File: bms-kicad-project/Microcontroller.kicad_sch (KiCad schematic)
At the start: 41 parts, among them J2 Conn_01x02, J3 USB_B_Micro, J4 Conn_02x18_Odd_Even, J5 Conn_02x18_Odd_Even, J6 12402012E212A, U2 NCP1117-3.3_SOT223, U3 W25Q128JVS, U4 RP2040, U5 NCP1117ST33T3G, U6 W25Q128JVSIQ TR, Y1 ABM8-272-T3

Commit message: feat: continuing work on MCU circuit
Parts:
- removed C10, C11: 10u, Capacitor_SMD:C_0805_2012Metric, symbol Device:C
- removed C27, C28: 1µ, FixedWing:CAPC2012X140N, symbol FixedWing:GCM21BR71C105KA58L
- removed J3: USB_B_Micro, RP2040_minimal:USB_Micro-B_Amphenol_10103594-0001LF_Horizontal_modified, symbol Connector:USB_B_Micro
- removed R30: DNF, Resistor_SMD:R_0402_1005Metric, symbol Device:R
- removed U2: NCP1117-3.3_SOT223, Package_TO_SOT_SMD:SOT-223-3_TabPin2, symbol Regulator_Linear:NCP1117-3.3_SOT223
- removed U6: W25Q128JVSIQ TR, FixedWing:SOIC_208MIL_WIN, symbol FixedWing:W25Q128JVSIQ_TR
- added CR1: MBR120VLSFT1G, FixedWing:DIOM3616X98N, symbol FixedWing:MBR120VLSFT1G
- added Q7: BSS308PE_H6327, SOT95P260X110-3N, symbol FixedWing:BSS308PE_H6327
- added R32, R33: 3k3, RESC2012X50N, symbol FixedWing:CRCW08053K30JNEA
- added R? (x4): 1k, FixedWing:RC0805N_YAG, symbol FixedWing:RC0805FR-071KL
- C?: renamed from C12; value 100n -> 0.1µ; footprint Capacitor_SMD:C_0402_1005Metric -> FixedWing:CAP_GCJ-18_MUR; symbol Device:C -> FixedWing:GCJ188R72A104KA01D; Manufacturer (none) -> Murata Electronics; Manufacturer_Part_Number (none) -> GCJ188R72A104KA01D
- C?: renamed from C16; value 100n -> 0.1µ; footprint Capacitor_SMD:C_0402_1005Metric -> FixedWing:CAP_GCJ-18_MUR; symbol Device:C -> FixedWing:GCJ188R72A104KA01D; Manufacturer (none) -> Murata Electronics; Manufacturer_Part_Number (none) -> GCJ188R72A104KA01D
- C?: renamed from C18; value 100n -> 0.1µ; footprint Capacitor_SMD:C_0402_1005Metric -> FixedWing:CAP_GCJ-18_MUR; symbol Device:C -> FixedWing:GCJ188R72A104KA01D; Manufacturer (none) -> Murata Electronics; Manufacturer_Part_Number (none) -> GCJ188R72A104KA01D
- C?: renamed from C19; value 100n -> 0.1µ; footprint Capacitor_SMD:C_0402_1005Metric -> FixedWing:CAP_GCJ-18_MUR; symbol Device:C -> FixedWing:GCJ188R72A104KA01D; Manufacturer (none) -> Murata Electronics; Manufacturer_Part_Number (none) -> GCJ188R72A104KA01D
- C?: renamed from C20; value 100n -> 0.1µ; footprint Capacitor_SMD:C_0402_1005Metric -> FixedWing:CAP_GCJ-18_MUR; symbol Device:C -> FixedWing:GCJ188R72A104KA01D; Manufacturer (none) -> Murata Electronics; Manufacturer_Part_Number (none) -> GCJ188R72A104KA01D
- C?: renamed from C21; value 100n -> 0.1µ; footprint Capacitor_SMD:C_0402_1005Metric -> FixedWing:CAP_GCJ-18_MUR; symbol Device:C -> FixedWing:GCJ188R72A104KA01D; Manufacturer (none) -> Murata Electronics; Manufacturer_Part_Number (none) -> GCJ188R72A104KA01D
- C?: renamed from C22; value 100n -> 0.1µ; footprint Capacitor_SMD:C_0402_1005Metric -> FixedWing:CAP_GCJ-18_MUR; symbol Device:C -> FixedWing:GCJ188R72A104KA01D; Manufacturer (none) -> Murata Electronics; Manufacturer_Part_Number (none) -> GCJ188R72A104KA01D
- C?: renamed from C23; value 100n -> 0.1µ; footprint Capacitor_SMD:C_0402_1005Metric -> FixedWing:CAP_GCJ-18_MUR; symbol Device:C -> FixedWing:GCJ188R72A104KA01D; Manufacturer (none) -> Murata Electronics; Manufacturer_Part_Number (none) -> GCJ188R72A104KA01D
- C?: renamed from C13; value 100n -> 0.1µ; footprint Capacitor_SMD:C_0402_1005Metric -> FixedWing:CAP_GCJ-18_MUR; symbol Device:C -> FixedWing:GCJ188R72A104KA01D; Manufacturer (none) -> Murata Electronics; Manufacturer_Part_Number (none) -> GCJ188R72A104KA01D
- C?: renamed from C14; value 100n -> 0.1µ; footprint Capacitor_SMD:C_0402_1005Metric -> FixedWing:CAP_GCJ-18_MUR; symbol Device:C -> FixedWing:GCJ188R72A104KA01D; Manufacturer (none) -> Murata Electronics; Manufacturer_Part_Number (none) -> GCJ188R72A104KA01D
- C?: renamed from C15; value 1u -> 1µ; footprint Capacitor_SMD:C_0402_1005Metric -> FixedWing:CAPC2012X140N; symbol Device:C -> FixedWing:GCM21BR71C105KA58L; Manufacturer (none) -> Murata Electronics; Manufacturer Part Number (none) -> GCM21BR71C105KA58L
- C?: renamed from C17; value 1u -> 1µ; footprint Capacitor_SMD:C_0402_1005Metric -> FixedWing:CAPC2012X140N; symbol Device:C -> FixedWing:GCM21BR71C105KA58L; Manufacturer (none) -> Murata Electronics; Manufacturer Part Number (none) -> GCM21BR71C105KA58L
- C?: renamed from C24; value 10u -> 10µ; footprint Capacitor_SMD:C_0805_2012Metric -> FixedWing:CAP_CL21B106KOQNNNE_SAM; symbol Device:C -> FixedWing:CL21B106KOQNNNE; Manufacturer (none) -> Samsung Electro-Mechanics; Manufacturer Part Number (none) -> CL21B106KOQNNNE
- R?: renamed from R29; footprint Resistor_SMD:R_0402_1005Metric -> FixedWing:RC0805N_YAG; symbol Device:R -> FixedWing:RC0805FR-071KL; Manufacturer (none) -> YAGEO; Manufacturer_Part_Number (none) -> RC0805FR-071KL
- R?: renamed from R32; footprint Resistor_SMD:R_0402_1005Metric -> FixedWing:RC0805N_YAG; symbol Device:R -> FixedWing:RC0805FR-0727RL; Manufacturer (none) -> YAGEO; Manufacturer_Part_Number (none) -> RC0805FR-0727RL
- R?: renamed from R33; footprint Resistor_SMD:R_0402_1005Metric -> FixedWing:RC0805N_YAG; symbol Device:R -> FixedWing:RC0805FR-0727RL; Manufacturer (none) -> YAGEO; Manufacturer_Part_Number (none) -> RC0805FR-0727RL
- R?: renamed from R31; footprint Resistor_SMD:R_0402_1005Metric -> FixedWing:RC0805N_YAG; symbol Device:R -> FixedWing:RC0805FR-071KL; Manufacturer (none) -> YAGEO; Manufacturer_Part_Number (none) -> RC0805FR-071KL
- U4: Manufacturer (none) -> Raspberry Pi; Manufacturer_Part_Number (none) -> SC0914(13)
- U?: renamed from U3; value W25Q128JVS -> W25Q128JVSIQ TR; footprint Package_SO:SOIC-8_5.23x5.23mm_P1.27mm -> FixedWing:SOIC_208MIL_WIN; symbol Memory_Flash:W25Q128JVS -> FixedWing:W25Q128JVSIQ_TR; Manufacturer (none) -> Winbond Electronics; Manufacturer_Part_Number (none) -> W25Q128JVSIQ TR
- renumbered J6 to J?, U5 to U?
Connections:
- net +1V1: now also C?.2, C?.2, C?.2; no longer C?.1, C?.1, C?.1
- net +3V3: now also C26.1, C?.2, C?.2, C?.2, C?.2, C?.2, C?.2, C?.2, C?.2, C?.2, C?.2, U?.2 (VO); no longer C?.1, C?.1, C?.1, C?.1, C?.1, C?.1, C?.1, C?.1, C?.1, C?.1
- net GND: now also C25.1, C26.2, C?.1, C?.1, C?.1, C?.1, C?.1, C?.1, C?.1, C?.1, C?.1, C?.1, C?.1, C?.1, C?.1, J?.A1_B12 (GND), J?.B1_A12 (GND__1), J?.SH1 (SHIELD), J?.SH2 (SHIELD__1), J?.SH3 (SHIELD__2), J?.SH4 (SHIELD__3), U?.1 (GND), R?.2, R?.2; no longer C?.2, C?.2, C?.2, C?.2, C?.2, C?.2, C?.2, C?.2, C?.2, C?.2, C?.2, C?.2, C?.2, U?.4 (GND)
- net QSPI_SS: now also R?.2; no longer R?.1
- net USB_D+: now also J?.A6 (D+_A), J?.B6 (D+_B), R?.2; no longer R?.1
- net USB_D-: now also J?.A7 (D-_A), J?.B7 (D-_B), R?.2; no longer R?.1
- net XOUT: now also R?.2; no longer R?.1
- net ~{USB_BOOT}: now also R?.1; no longer R?.2
- net at U4.46 (USB_DM): now also R?.1; no longer R?.2
- net at U4.47 (USB_DP): now also R?.1; no longer R?.2
- net at J?.A4_B9 (VBUS): now also J?.B4_A9 (VBUS__1), CR1.2, Q7.1 (G)
- net at J?.A5 (CC1_A): now also R33.1
- net at J?.B5 (CC1_B): now also R32.1
- net at C9.1, Y1.3: now also R?.1; no longer R?.2
- net at C25.2: now also U?.3 (VI), CR1.1, Q7.2 (S)
- new net: R33.2, R?.1
- new net: R?.1, R?.2 (x2)
- new net: R32.2, R?.1
- new net +5V: Q7.3 (D)
- no-connect marks 1 -> 2
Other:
- note added: "MCU"
- note removed: "Make sure C10 is close to pin 44 of RP2040"
- note removed: "Make sure C8 is close to pin 45 of RP2040"
- note removed: "Make sure R3 and R4 are close to RP2040"
- note removed: "WIP"
- moved on the sheet: C25, C26, C8, C9, H1, H2, H3, H4, J2, J4, J5, J?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

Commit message: feat: finished preliminary RP2040 schematic design
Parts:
- removed H1, H2, H3, H4: MountingHole, MountingHole:MountingHole_2.7mm_M2.5, symbol Mechanical:MountingHole
- removed J2: Conn_01x02, Connector_PinHeader_2.54mm:PinHeader_1x02_P2.54mm_Vertical, symbol Connector_Generic:Conn_01x02
- added J?: DEBUG, Connector_PinHeader_2.54mm:PinHeader_1x03_P2.54mm_Vertical, symbol Connector_Generic:Conn_01x03
- added R29: 3k3, RESC2012X50N, symbol FixedWing:CRCW08053K30JNEA
- added SW1, SW2: KMR223G LFG, FixedWing:KMR2_G_CNK, symbol FixedWing:KMR223G_LFG
- C?: renamed from C8; footprint Capacitor_SMD:C_0402_1005Metric -> FixedWing:CAPC2012X70; symbol Device:C -> FixedWing:CC0805JPNPO9BN150; Manufacturer (none) -> YAGEO; Manufacturer_Part_Number (none) -> CC0805JPNPO9BN150
- C?: renamed from C9; footprint Capacitor_SMD:C_0402_1005Metric -> FixedWing:CAPC2012X70; symbol Device:C -> FixedWing:CC0805JPNPO9BN150; Manufacturer (none) -> YAGEO; Manufacturer_Part_Number (none) -> CC0805JPNPO9BN150
- U?: renamed from U4; Tutorial (none) -> https://datasheets.raspberrypi.com/rp2040/hardware-design-w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
- X?: renamed from Y1; footprint Crystal:Crystal_SMD_3225-4Pin_3.2x2.5mm -> FixedWing:ABM8-272-T3_ABR; symbol Device:Crystal_GND24 -> FixedWing:ABM8-272-T3; Manufacturer (none) -> Abracon LLC; Manufacturer_Part_Number (none) -> ABM8-272-T3
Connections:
- net +1V1: no longer U?.23 (DVDD), U?.50 (DVDD)
- net +3V3: now also R29.2; no longer U?.1 (IOVDD), U?.10 (IOVDD), U?.22 (IOVDD), U?.33 (IOVDD), U?.42 (IOVDD), U?.43 (ADC_AVDD), U?.48 (USB_VDD), U?.49 (IOVDD)
- net GND: now also C?.1, C?.1, J?.2 (Pin_2), SW1.3, SW1.4, SW1.5, SW2.3, SW2.4, SW2.5; no longer C?.2, C?.2
- net RUN: no longer U?.26 (RUN)
- net SWCLK: now also J?.1 (Pin_1)
- net SWD: now also J?.3 (Pin_3)
- net XIN: now also C?.2; no longer C?.1
- net ~{USB_BOOT}: now also SW1.1, SW1.2
- net at R?.1, X?.3: now also C?.2; no longer C?.1
- net GPIO0 renamed SPI0_RX
- net GPIO1 renamed SPI0_CSn
- net GPIO2 renamed SPI0_SCK
- net GPIO3 renamed SPI0_TX
- new net ~{RESET}: R29.1, SW2.1, SW2.2, U?.26 (RUN)
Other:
- note added: "Reset"
- moved on the sheet: C25, C26, C?, CR1, J4, J5, J?, Q7, R32, R33, R?, U?

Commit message: Feature: Added schematic and symbols for 5V switching regulator (#16)
* feat: initial 5V-reg-and-edits branch commit

* feat: small to-do list edits

* feat: put filtering and balancing circuits into hierarchical format

* feat: forgot to commit smol change

* feat: Added SiC461 Schematic, Footprint, and 3D Model

* feat: Added all components listed in the spreadsheet, until Inductor L1

* feat: forgor the description

* feat: Added all symbols and 3D models. Also began working on Regulator Schematic.

* feat: Added more connections to the 5V Regulator schematic.

* feat: Added VFB connection in 5V Regulator Schematic

* feat: Added 220uf cap & modified 5V Reg Circuit

* feat: Added more to 5V Regulator Schematic

* feat: Changed all resistor symbols to be the standard KiCAD symbol, started improving schematic.

* feat: Forgot to save changes to schematic.

* feat: Just about completed 5V Regulator Schematic.

* feat: cosmetic changes to 5V reg schematic

* feat: Added comment boxes and fixed 5V Regulator Schematic.

* feat: just moved around and edited notes on the 5V reg schematic

* feat: re-ordered page numbers

* feat: Added snubber circuit to 5V Regulator schematic

* feat: Added 0OHM jumper between ULTRASONIC and VDD, added LED indicator for PGOOD

* feat: added buncha shit, refer to tasks 4 and 8

* feat: finished 5V reg circuit lgtm!

---------

Co-authored-by: cowman19 <matthewf9001@gmail.com>
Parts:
- removed R29, R32, R33: 3k3, RESC2012X50N, symbol FixedWing:CRCW08053K30JNEA
- removed R? (x4): 1k, FixedWing:RC0805N_YAG, symbol FixedWing:RC0805FR-071KL
- added R77, R78, R81: 5.6k, FixedWing:RESC2012X60N, symbol FixedWing:RK73H2ATTD5601F
- gave numbers to parts that had none: 25
- renumbered C25 to C18, C26 to C19, J4 to J3, J5 to J4, Q7 to Q13, SW2 to SW1, SW1 to SW2
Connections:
- net +3V3: now also C17.1, C19.2, C24.1, C26.1, C28.1, C29.1, C30.1, C31.1, R81.1; no longer C17.2, C19.1, C24.2, C26.2, C28.2, C29.2, C30.2, C31.2
- net GND: now also C17.2, C18.2, C19.1, C24.2, C26.2, C28.2, C29.2, C30.2, C31.2, R77.1, R78.1; no longer C17.1, C18.1, C19.2, C24.1, C26.1, C28.1, C29.1, C30.1, C31.1
- net ~{RESET}: now also R81.2
- net at J1.A5 (CC1_A): now also R78.2
- net at J1.B5 (CC1_B): now also R77.2
- net at CR1.1, Q13.2 (S), U3.3 (VI): now also C18.1; no longer C18.2
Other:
- company: (none) -> AeroNU - FixedWing
- moved on the sheet: C18, C19

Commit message: feat: making sure my git still works
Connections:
- net +1V1: now also U4.23 (DVDD), U4.50 (DVDD)
- net +3V3: now also U4.1 (IOVDD), U4.10 (IOVDD), U4.22 (IOVDD), U4.33 (IOVDD), U4.42 (IOVDD), U4.43 (ADC_AVDD), U4.48 (USB_VDD), U4.49 (IOVDD)
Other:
- moved on the sheet: C21, C22

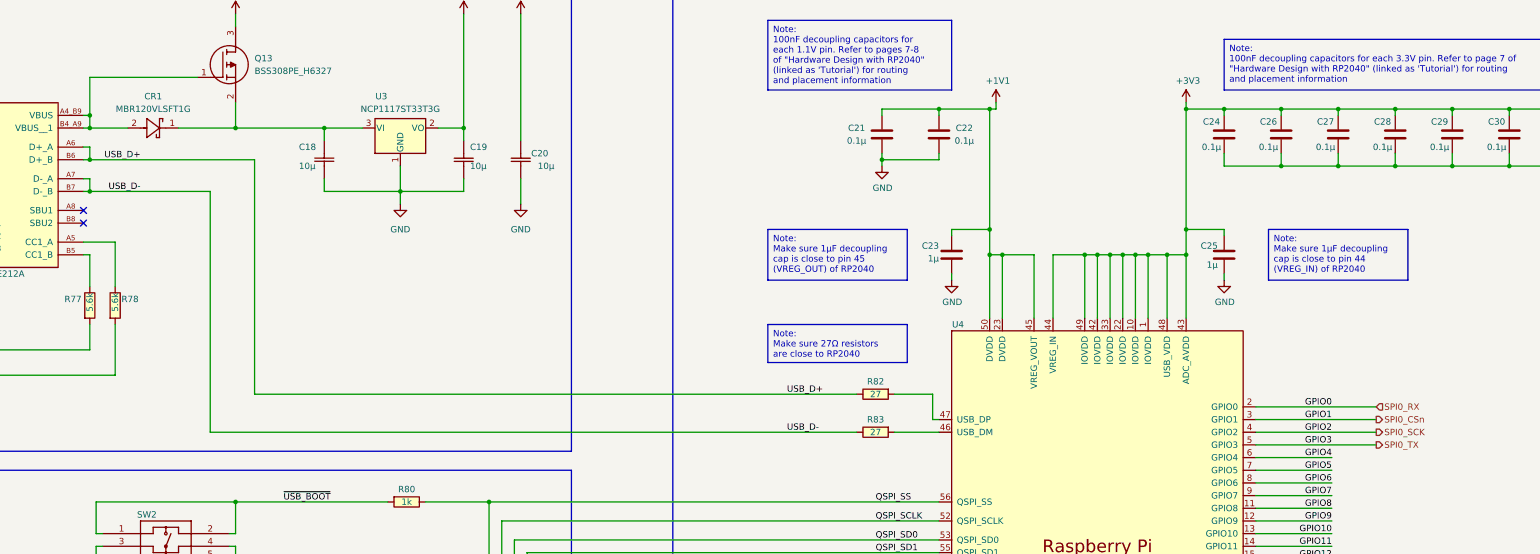
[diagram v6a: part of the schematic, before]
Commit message: feat: figured out battery stack monitor V+ biasing. Refer to task 5 on the punchlist for more details.
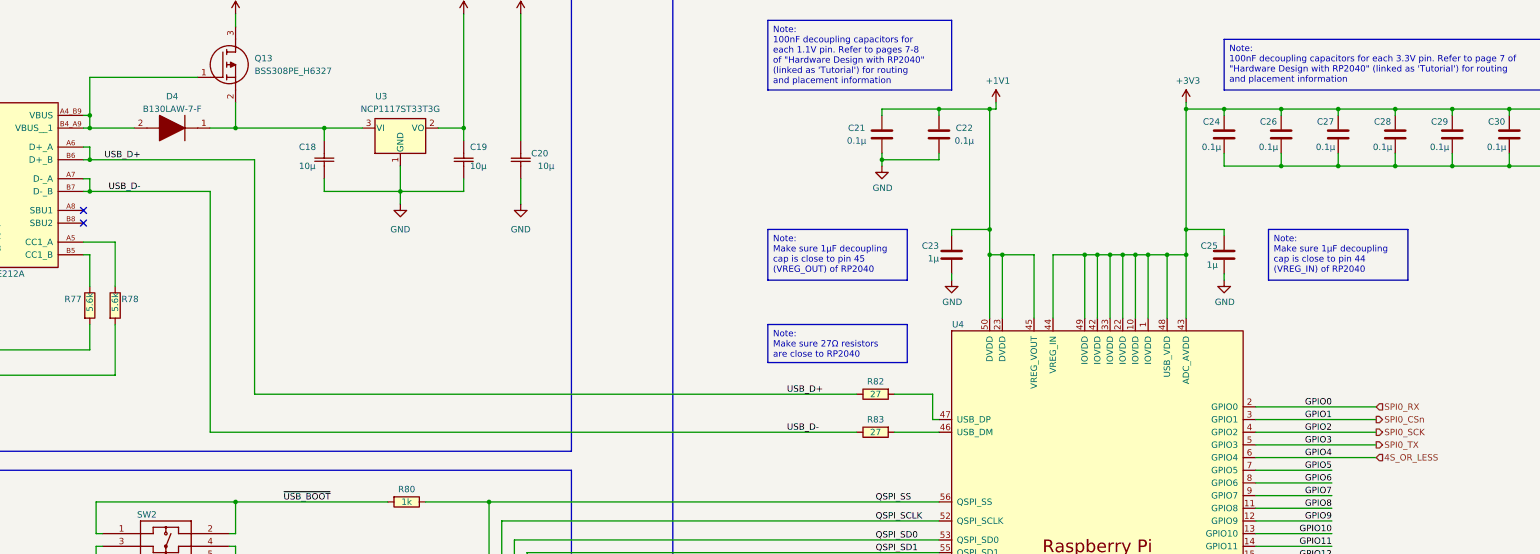
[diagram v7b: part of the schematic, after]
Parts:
- removed CR1: MBR120VLSFT1G, FixedWing:DIOM3616X98N, symbol FixedWing:MBR120VLSFT1G
- added D4: B130LAW-7-F, FixedWing:SOD3716X145N, symbol FixedWing:B130LAW-7-F
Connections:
- net at J1.A4_B9 (VBUS), J1.B4_A9 (VBUS__1), Q13.1 (G): now also D4.2 (A)
- net at C18.1, Q13.2 (S), U3.3 (VI): now also D4.1 (K)
- net GPIO4 renamed 4S_OR_LESS
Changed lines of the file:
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@@
     (stroke (width 0) (type default))
   )
+  (wire (pts (xy 78.74 46.99) (xy 83.82 46.99))
+    (stroke (width 0) (type default))
+  )
   (wire (pts (xy 274.32 72.39) (xy 274.32 85.09))
     (stroke (width 0) (type default))
@@
     (stroke (width 0) (type default))
   )
-  (wire (pts (xy 72.39 46.99) (xy 83.82 46.99))
-    (stroke (width 0) (type default))
-  )
   (wire (pts (xy 406.4 158.75) (xy 393.7 158.75))
     (stroke (width 0) (type default))
@@
     (stroke (width 0) (type default))
   )
-  (wire (pts (xy 54.61 46.99) (xy 62.23 46.99))
+  (wire (pts (xy 54.61 46.99) (xy 63.5 46.99))
     (stroke (width 0) (type default))
   )
@@
     (stroke (width 0) (type default))
   )
-  (wire (pts (xy 288.29 113.03) (xy 303.53 113.03))
+  (wire (pts (xy 288.29 113.03) (xy 312.42 113.03))
     (stroke (width 0) (type default))
   )
@@
     (effects (font (size 1.27 1.27)) (justify left))
   )
+  (hierarchical_label "4S_OR_LESS" (shape input) (at 312.42 113.03 0) (fields_autoplaced)
+    (effects (font (size 1.27 1.27)) (justify left))
+  )
   (hierarchical_label "SPI0_CSn" (shape output) (at 312.42 105.41 0) (fields_autoplaced)
     (effects (font (size 1.27 1.27)) (justify left))
@@
     )
   )
-  (symbol (lib_id "FixedWing:MBR120VLSFT1G") (at 62.23 46.99 0) (unit 1)
-    (in_bom yes) (on_board yes) (dnp no) (fields_autoplaced)
-    (property "Reference" "CR1" (at 67.31 40.64 0)
-      (effects (font (size 1.27 1.27)))
-    )
-    (property "Value" "MBR120VLSFT1G" (at 67.31 43.18 0)
-      (effects (font (size 1.27 1.27)))
-    )
-    (property "Footprint" "FixedWing:DIOM3616X98N" (at 62.23 46.99 0)
-      (effects (font (size 1.27 1.27) italic) hide)
-    )
-    (property "Datasheet" "https://www.onsemi.com/pdf/datasheet/mbr120vlsft1-d.pdf" (at 62.23 46.99 0)
-      (effects (font (size 1.27 1.27) italic) hide)
-    )
-    (property "Manufacturer" "onsemi" (at 62.23 46.99 0)
-      (effects (font (size 1.27 1.27)) hide)
-    )
-    (property "Manufacturer_Part_Number" "MBR120VLSFT1G" (at 62.23 46.99 0)
-      (effects (font (size 1.27 1.27)) hide)
-    )
-    (pin "1")
-    (pin "2")
-    (instances
-      (project "bms-board"
-        (path "/8a7831d1-a913-4f04-8780-225d2234b41d/449bb263-23d7-4f07-b4f7-6cd2e161d267"
-          (reference "CR1") (unit 1)
-        )
-      )
-    )
-  )
   (symbol (lib_id "FixedWing:RK73H2ATTD5601F") (at 54.61 86.36 90) (unit 1)
     (in_bom yes) (on_board yes) (dnp no)
@@
         )
       )
+    )
+  )
+  (symbol (lib_id "FixedWing:B130LAW-7-F") (at 78.74 46.99 180) (unit 1)
+    (in_bom yes) (on_board yes) (dnp no)
+    (property "Reference" "D4" (at 71.12 40.64 0)
+      (effects (font (size 1.27 1.27)))
+    )
+    (property "Value" "B130LAW-7-F" (at 71.12 43.18 0)
+      (effects (font (size 1.27 1.27)))
+    )
+    (property "Footprint" "FixedWing:SOD3716X145N" (at 67.31 -50.47 0)
+      (effects (font (size 1.27 1.27)) (justify left top) hide)
+    )
+    (property "Datasheet" "https://www.diodes.com//assets/Datasheets/B130LAW.pdf" (at 67.31 -150.47 0)
+      (effects (font (size 1.27 1.27)) (justify left top) hide)
+    )
+    (property "Height" "1.45" (at 67.31 -350.47 0)
+      (effects (font (size 1.27 1.27)) (justify left top) hide)
+    )
+    (property "Manufacture" "Diodes Incorporated" (at 67.31 -450.47 0)
+      (effects (font (size 1.27 1.27)) (justify left top) hide)
+    )
+    (property "Manufacturer Part Number" "B130LAW-7-F" (at 67.31 -550.47 0)
+      (effects (font (size 1.27 1.27)) (justify left top) hide)
+    )
+    (property "Mouser Part Number" "621-B130LAW-F" (at 67.31 -650.47 0)
+      (effects (font (size 1.27 1.27)) (justify left top) hide)
+    )
+    (property "Mouser Price/Stock" "https://www.mouser.co.uk/ProductDetail/Diodes-Incorporated/B130LAW-7-F?qs=N%2F0WmOHT%2Fs7skU1ebzJOew%3D%3D" (at 67.31 -750.47 0)
+      (effects (font (size 1.27 1.27)) (justify left top) hide)
+    )
+    (property "Arrow Part Number" "B130LAW-7-F" (at 67.31 -850.47 0)
+      (effects (font (size 1.27 1.27)) (justify left top) hide)
+    )
+    (property "Arrow Price/Stock" "https://www.arrow.com/en/products/b130law-7-f/diodes-incorporated?utm_currency=USD&region=europe" (at 67.31 -950.47 0)
+      (effects (font (size 1.27 1.27)) (justify left top) hide)
+    )
+    (pin "2")
+    (pin "1")
+    (instances
+      (project "bms-board"
+        (path "/8a7831d1-a913-4f04-8780-225d2234b41d/449bb263-23d7-4f07-b4f7-6cd2e161d267"
+          (reference "D4") (unit 1)
+        )
+      )
